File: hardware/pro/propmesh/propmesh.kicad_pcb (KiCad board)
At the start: 2 copper layers, 33 parts, among them J1 DC_IN, J2 DC_JACK, Q2 AOD4185, U1 TLV62569DBV, U2 AP64350SP-13

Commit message: Sheet 03 (slow outputs) captured + channel redesign to supply voltage
- LED-channel decision resolved: all 6 channels kept, discrete AO3400A
  low-side FETs (Basic, replaces sheet 06's 2N7002 too — one MOSFET
  part number board-wide); ULN2003 drives relays only
- Channels re-pointed +5V -> VIN_PROT with SS34 flyback per channel:
  2 A/ch, 5 A aggregate, 12/24 V lights and pneumatic solenoids are
  first-class loads. Supply-voltage coupling documented in the spec's
  user guidance (match supply to lights; mixed-voltage recipe)
- HK4100F relay: symbol+footprint imported, land pattern verified,
  EasyEDA inverted-pin defect fixed in library (4th known import lie,
  added to checklist); coil is 40 mA not 70; NO/NC continuity check
  deferred to bring-up by design
- checknet renderer: undrawn power rails annotate inside part boxes
  (no more +5V hairball); roll-call generalised
- All three drawn sheets: checknet green, ERC clean (31 one-sided
  labels pending sheets 04-07). Caught U3's footprint reverted to
  WROOM-1 by Update-from-Library field reset — reassigned, dialog
  gotcha documented

Co-Authored-By: Claude Fable 5 <noreply@anthropic.com>
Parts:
- added C13: 1u, Capacitor_SMD:C_0603_1608Metric, F.Cu at (149.2, 22.0)
- added C14: 100n, Capacitor_SMD:C_0603_1608Metric, F.Cu at (152.4, 26.7)
- added C15: 10u/16V, Capacitor_SMD:C_0805_2012Metric, F.Cu at (152.6, 52.8)
- added C16: 10U, Capacitor_SMD:C_0805_2012Metric, F.Cu at (253.6, 140.9)
- added C17: 100n, Capacitor_SMD:C_0603_1608Metric, F.Cu at (249.4, 117.7)
- added D10: SS34, Diode_SMD:D_SMA, F.Cu at (238.4, 136.9)
- added D11: SS34, Diode_SMD:D_SMA, F.Cu at (238.4, 141.4)
- added D5: SS34, Diode_SMD:D_SMA, F.Cu at (145.6, 46.4)
- added D6: SS34, Diode_SMD:D_SMA, F.Cu at (238.4, 118.7)
- added D7: SS34, Diode_SMD:D_SMA, F.Cu at (238.4, 123.2)
- added D8: SS34, Diode_SMD:D_SMA, F.Cu at (238.4, 127.8)
- added D9: SS34, Diode_SMD:D_SMA, F.Cu at (238.4, 132.3)
- added J10: SERVO, Connector_PinHeader_2.54mm:PinHeader_1x03_P2.54mm_Vertical, F.Cu at (245.8, 109.0)
- added J11: SERVO, Connector_PinHeader_2.54mm:PinHeader_1x03_P2.54mm_Vertical, F.Cu at (250.4, 109.0)
- added J12: SERVO, Connector_PinHeader_2.54mm:PinHeader_1x03_P2.54mm_Vertical, F.Cu at (255.0, 109.0)
- added J13: SERVO, Connector_PinHeader_2.54mm:PinHeader_1x03_P2.54mm_Vertical, F.Cu at (259.6, 109.0)
- added J3: RELAY_OUT, propmesh:CONN-TH_DG128-5.0-03P-14-00A-H, F.Cu at (226.2, 112.4)
- added J4: TYPE-C-31-M-12, Connector_USB:USB_C_Receptacle_HRO_TYPE-C-31-M-12, F.Cu at (127.0, 49.0)
- added J6: RELAY_OUT, propmesh:CONN-TH_DG128-5.0-03P-14-00A-H, F.Cu at (226.2, 123.8)
- added J7: SERVO, Connector_PinHeader_2.54mm:PinHeader_1x03_P2.54mm_Vertical, F.Cu at (236.7, 109.0)
- added J8: RELAY_OUT, propmesh:CONN-TH_DG128-5.0-03P-14-00A-H, F.Cu at (226.2, 135.3)
- added J9: SERVO, Connector_PinHeader_2.54mm:PinHeader_1x03_P2.54mm_Vertical, F.Cu at (241.2, 109.0)
- added J_LED1: LED_OUT, propmesh:CONN-TH_DG381S-3.5-02P-14-00A-H, F.Cu at (204.9, 100.4)
- added J_LED2: LED_OUT, propmesh:CONN-TH_DG381S-3.5-02P-14-00A-H, F.Cu at (213.6, 100.4)
- added J_LED3: LED_OUT, propmesh:CONN-TH_DG381S-3.5-02P-14-00A-H, F.Cu at (222.4, 100.4)
- added J_LED4: LED_OUT, propmesh:CONN-TH_DG381S-3.5-02P-14-00A-H, F.Cu at (231.1, 100.4)
- added J_LED5: LED_OUT, propmesh:CONN-TH_DG381S-3.5-02P-14-00A-H, F.Cu at (239.9, 100.4)
- added J_LED6: LED_OUT, propmesh:CONN-TH_DG381S-3.5-02P-14-00A-H, F.Cu at (248.6, 100.4)
- added K1: HK4100F-DC5V-SHG, propmesh:RELAY-TH_HK4100F-DC5V-SHG, F.Cu at (209.2, 112.9)
- added K2: HK4100F-DC5V-SHG, propmesh:RELAY-TH_HK4100F-DC5V-SHG, F.Cu at (209.2, 125.3)
- added K3: HK4100F-DC5V-SHG, propmesh:RELAY-TH_HK4100F-DC5V-SHG, F.Cu at (209.2, 137.6)
- added Q1: AO3400A, Package_TO_SOT_SMD:SOT-23, F.Cu at (244.9, 118.6)
- added Q3: AO3400A, Package_TO_SOT_SMD:SOT-23, F.Cu at (244.9, 123.1)
- added Q4: AO3400A, Package_TO_SOT_SMD:SOT-23, F.Cu at (244.9, 127.5)
- added Q5: AO3400A, Package_TO_SOT_SMD:SOT-23, F.Cu at (244.9, 132.0)
- added Q6: AO3400A, Package_TO_SOT_SMD:SOT-23, F.Cu at (244.9, 136.4)
- added Q7: AO3400A, Package_TO_SOT_SMD:SOT-23, F.Cu at (244.9, 140.9)
- added R10: 5.1k, Resistor_SMD:R_0603_1608Metric, F.Cu at (152.4, 29.2)
- added R11: 5.1k, Resistor_SMD:R_0603_1608Metric, F.Cu at (152.4, 31.7)
- added R12: 10k, Resistor_SMD:R_0603_1608Metric, F.Cu at (152.4, 34.2)
- added R13: 10k, Resistor_SMD:R_0603_1608Metric, F.Cu at (152.4, 36.7)
- added R14: 10k, Resistor_SMD:R_0603_1608Metric, F.Cu at (249.4, 120.2)
- added R15: 10k, Resistor_SMD:R_0603_1608Metric, F.Cu at (249.4, 122.7)
- added R16: 10k, Resistor_SMD:R_0603_1608Metric, F.Cu at (249.4, 125.2)
- added R17: 10k, Resistor_SMD:R_0603_1608Metric, F.Cu at (249.4, 127.7)
- added R18: 10k, Resistor_SMD:R_0603_1608Metric, F.Cu at (249.4, 130.2)
- added R19: 10k, Resistor_SMD:R_0603_1608Metric, F.Cu at (249.4, 132.7)
- added R20: 4.7k, Resistor_SMD:R_0603_1608Metric, F.Cu at (249.4, 135.2)
- added R21: 4.7k, Resistor_SMD:R_0603_1608Metric, F.Cu at (249.4, 137.8)
- added SW1: TS-1187A, Button_Switch_SMD:SW_Push_1P1T_XKB_TS-1187A, F.Cu at (171.5, 41.3)
- added SW2: TS-1187A, Button_Switch_SMD:SW_Push_1P1T_XKB_TS-1187A, F.Cu at (172.5, 54.5)
- added TP1: TP37, TestPoint:TestPoint_Pad_1.5x1.5mm, F.Cu at (148.4, 50.4)
- added U3: ESP32-S3-WROOM-1U-N8R2, RF_Module:ESP32-S3-WROOM-1U, F.Cu at (132.0, 24.7)
- added U4: USBLC6-2SC6, Package_TO_SOT_SMD:SOT-23-6, F.Cu at (144.1, 51.1)
- added U5: PCA9685PW, Package_SO:TSSOP-28_4.4x9.7mm_P0.65mm, F.Cu at (255.7, 133.8)
- added U6: ULN2003A, Package_SO:SOIC-16_3.9x9.9mm_P1.27mm, F.Cu at (255.6, 122.3)
- moved J2 34.6 mm to (18.9, 27.5)
- moved J1 22.3 mm to (18.0, 39.5), turned to -90 degrees
- moved F1 18.1 mm to (27.3, 10.3)
- moved C2 14.1 mm to (17.0, 51.0)
- moved Q2 12.9 mm to (46.8, 70.1)

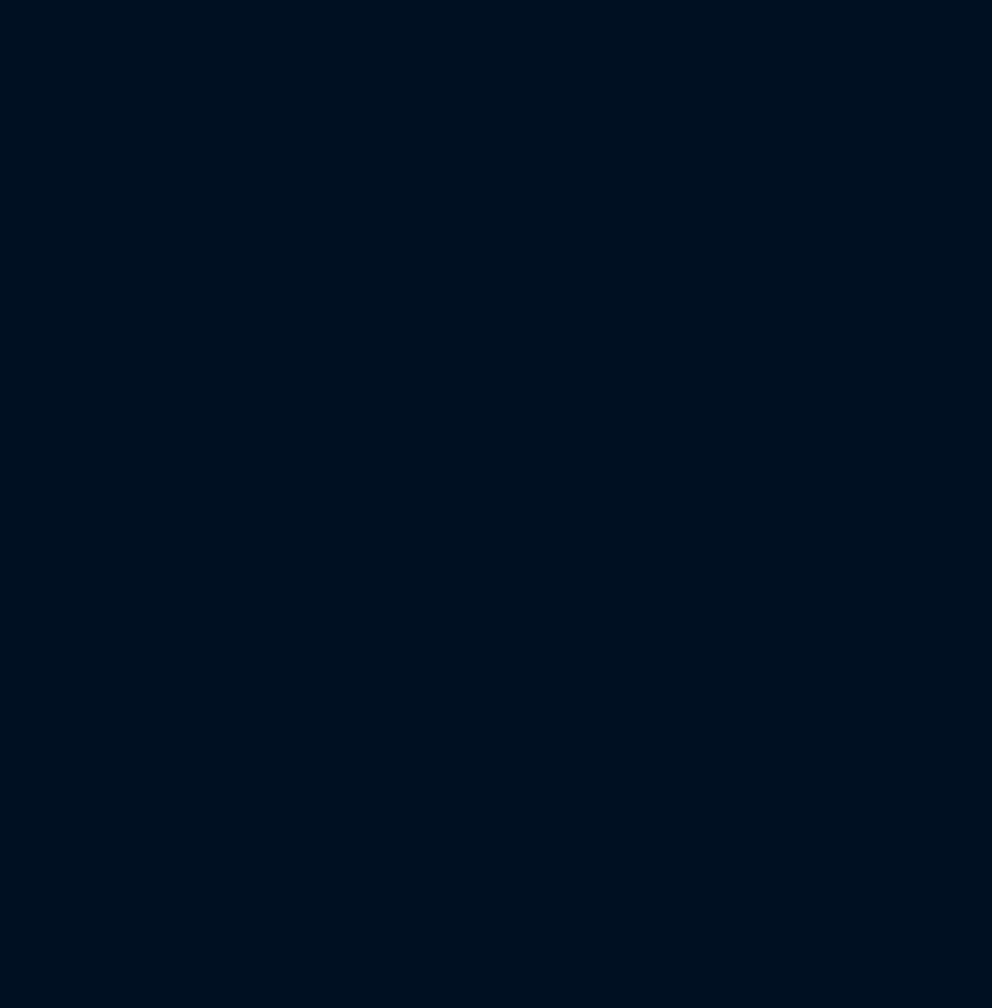
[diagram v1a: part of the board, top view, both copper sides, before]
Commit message: Sheet 04 (audio + SD) captured: mono amp, PCM5102A line-out, microSD
- MAX98357A config resolved datasheet-exact: GAIN_SLOT->GND = 12 dB
  (zero parts); SD_MODE mono mix via 620k to +3V3 (RLARGE formula,
  window computed vs trip points; rail chosen for noise margin and
  the one-rail strap convention). Genuine ADI $0.88@100 dissolved
  the clone question.
- Line-out dropped then REVERSED same day (Colin): PCM5102A second
  DAC on the shared I2S bus, TI Fig.33 literal (SCK grounded = BCK
  PLL), 470R+2.2nF outputs, PJ-320A jack. ~$1.65 for the honest
  version; audio block $3.28@100 verified vs $2.65 estimate.
- PJ-320A mapping settled by geometry after THREE numbering schemes
  collided (datasheet contacts 1-4, import pads 2-5, unnumbered PCB
  layout): L=4 (deepest spring = tip, Colin's argument), R=3,
  GND=2+5. Meter-confirm at bring-up. Import-lie #5 documented.
- microSD TF-01A with D3 pull-up ADDED beyond the pinmap note
  (ESP-IDF: D3 low drops the card into SPI mode); card-detect to a
  test pad.
- Library: pin types set on all four audio imports (amp NC pins
  typed no_connect); peg-hole NPTH fixes on TF-01A and PJ-320A.
- checknet renderer: rail-only parts (pure decoupling) now render in
  their own diagram section — ten invisible caps taught us the
  drawing guide could silently drop parts.
- All four drawn sheets: checknet green, ERC clean.

Co-Authored-By: Claude Fable 5 <noreply@anthropic.com>
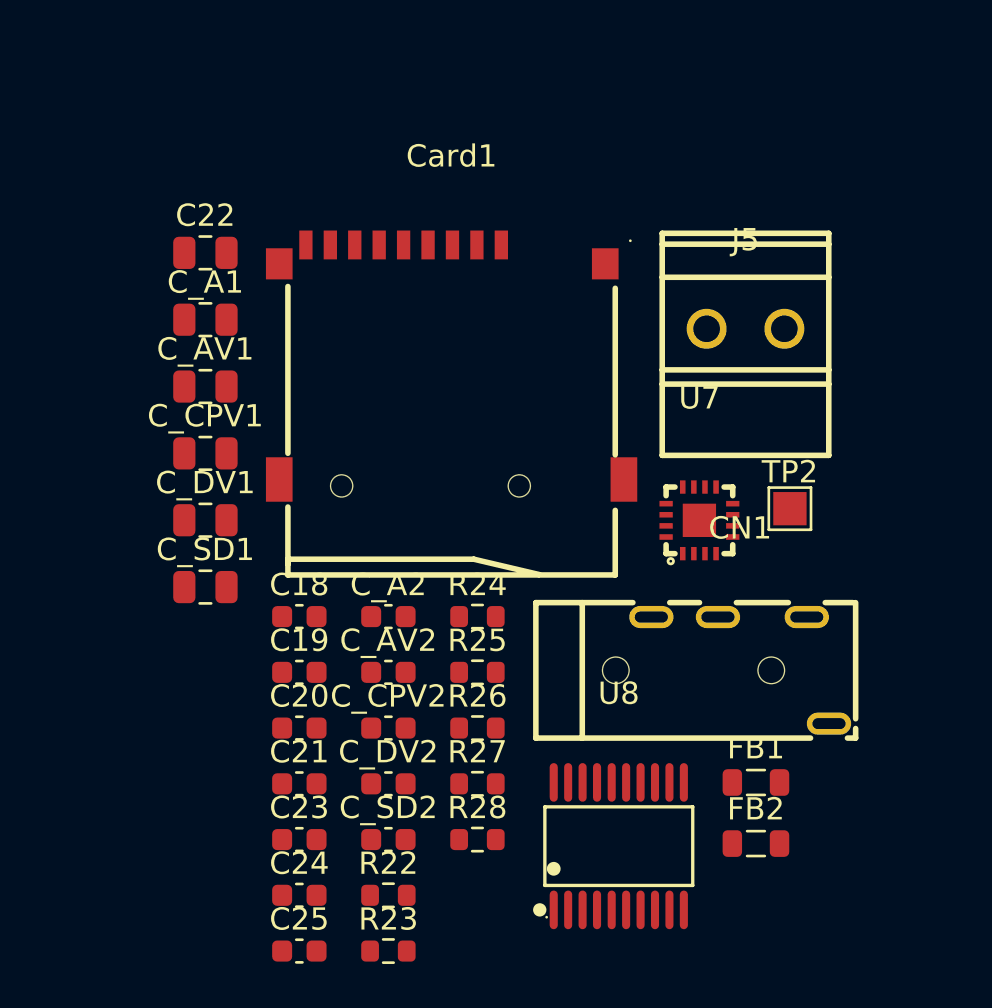
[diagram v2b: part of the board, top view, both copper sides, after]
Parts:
- added C18: 100p, Capacitor_SMD:C_0603_1608Metric, F.Cu at (33.0, 169.4)
- added C19: 100p, Capacitor_SMD:C_0603_1608Metric, F.Cu at (33.0, 171.9)
- added C20: 2.2u, Capacitor_SMD:C_0603_1608Metric, F.Cu at (33.0, 174.4)
- added C21: 2.2u, Capacitor_SMD:C_0603_1608Metric, F.Cu at (33.0, 176.9)
- added C22: 10u, Capacitor_SMD:C_0805_2012Metric, F.Cu at (28.7, 153.0)
- added C23: 100n, Capacitor_SMD:C_0603_1608Metric, F.Cu at (33.0, 179.4)
- added C24: 2.2n, Capacitor_SMD:C_0603_1608Metric, F.Cu at (33.0, 181.9)
- added C25: 2.2n, Capacitor_SMD:C_0603_1608Metric, F.Cu at (33.0, 184.4)
- added CN1: LINE_OUT, propmesh:AUDIO-TH_XKB_PJ-320A, F.Cu at (52.8, 171.8)
- added C_A1: 10u, Capacitor_SMD:C_0805_2012Metric, F.Cu at (28.7, 156.0)
- added C_A2: 100n, Capacitor_SMD:C_0603_1608Metric, F.Cu at (37.0, 169.4)
- added C_AV1: 10u, Capacitor_SMD:C_0805_2012Metric, F.Cu at (28.7, 159.0)
- added C_AV2: 100n, Capacitor_SMD:C_0603_1608Metric, F.Cu at (37.0, 171.9)
- added C_CPV1: 10u, Capacitor_SMD:C_0805_2012Metric, F.Cu at (28.7, 162.0)
- added C_CPV2: 100n, Capacitor_SMD:C_0603_1608Metric, F.Cu at (37.0, 174.4)
- added C_DV1: 10u, Capacitor_SMD:C_0805_2012Metric, F.Cu at (28.7, 165.0)
- added C_DV2: 100n, Capacitor_SMD:C_0603_1608Metric, F.Cu at (37.0, 176.9)
- added C_SD1: 10u, Capacitor_SMD:C_0805_2012Metric, F.Cu at (28.7, 168.1)
- added C_SD2: 100n, Capacitor_SMD:C_0603_1608Metric, F.Cu at (37.0, 179.4)
- added Card1: TF-01A, propmesh:TF-SMD_TF-01A, F.Cu at (39.8, 157.9)
- added FB1: BLM21PG221SN1D, Inductor_SMD:L_0805_2012Metric, F.Cu at (53.5, 176.9)
- added FB2: BLM21PG221SN1D, Inductor_SMD:L_0805_2012Metric, F.Cu at (53.5, 179.6)
- added J5: SPEAKER, propmesh:CONN-TH_DG381S-3.5-02P-14-00A-H, F.Cu at (53.0, 156.4)
- added R22: 620K, Resistor_SMD:R_0603_1608Metric, F.Cu at (37.0, 181.9)
- added R23: 10k, Resistor_SMD:R_0603_1608Metric, F.Cu at (37.0, 184.4)
- added R24: 470, Resistor_SMD:R_0603_1608Metric, F.Cu at (41.0, 169.4)
- added R25: 470, Resistor_SMD:R_0603_1608Metric, F.Cu at (41.0, 171.9)
- added R26: 10k, Resistor_SMD:R_0603_1608Metric, F.Cu at (41.0, 174.4)
- added R27: 10k, Resistor_SMD:R_0603_1608Metric, F.Cu at (41.0, 176.9)
- added R28: 10k, Resistor_SMD:R_0603_1608Metric, F.Cu at (41.0, 179.4)
- added TP2: TP_CD, TestPoint:TestPoint_Pad_1.5x1.5mm, F.Cu at (55.0, 164.5)
- added U7: MAX98357AETE+T, propmesh:TQFN-16_L3.0-W3.0-P0.50-BL-EP1.5, F.Cu at (51.0, 165.1)
- added U8: PCM5102APWR, propmesh:TSSOP-20_L6.5-W4.4-P0.65-LS6.4-BL, F.Cu at (47.3, 179.7)

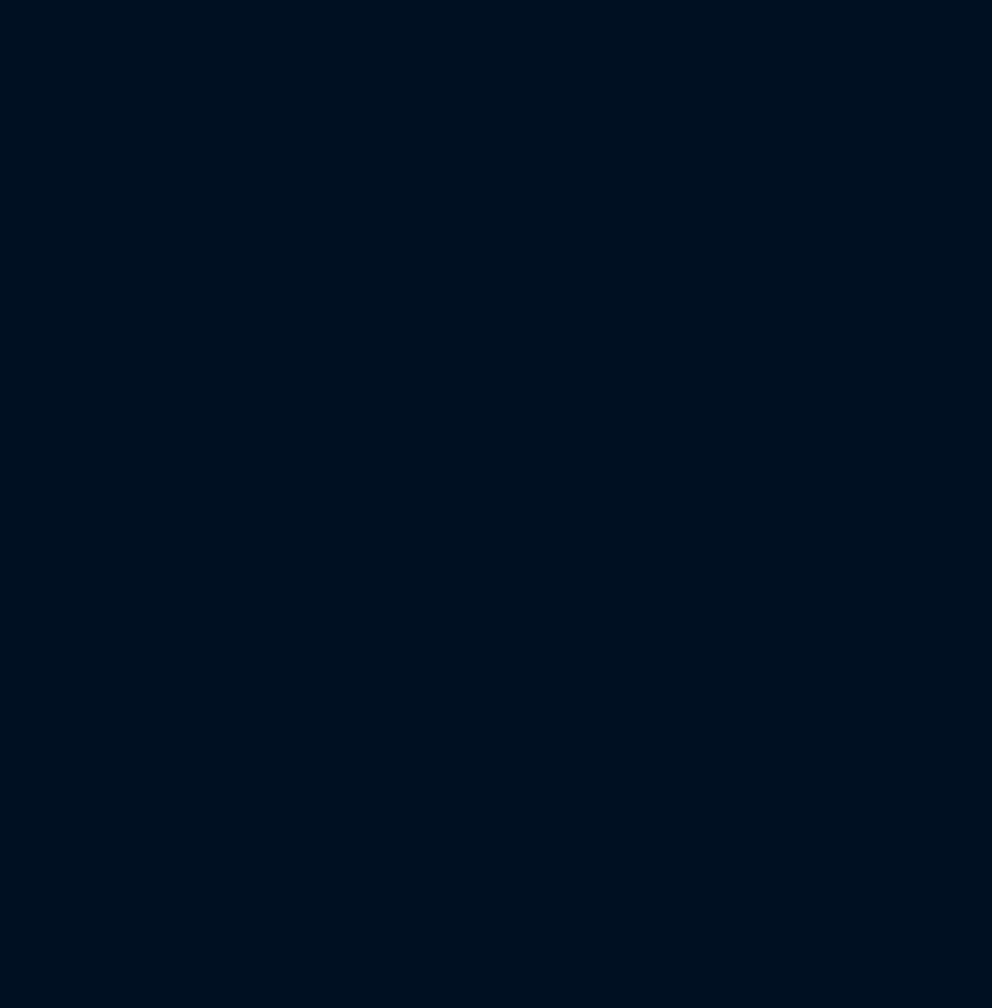
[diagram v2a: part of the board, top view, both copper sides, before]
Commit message: Sheet 06 (motors) captured: stepper sockets + DRV8871, all spec unknowns closed
- Open item #3 CLOSED from the Pololu md09b drawing: StepStick rows
  12.70 mm apart exactly, 1x8 @ 2.54; RST/SLP positions hardwired
  together = A4988-legal AND the TMC2209 PDN_UART bus (shared, both
  sockets, MS1/MS2 straps = addresses); DIAG via per-socket aux
  headers + bridged solder jumpers (vendor positions differ);
  1k series on GPIO43 (U0TXD boot log)
- ILIM verified from TI DS: ITRIP = 64000/R; 30k = 2.13 A/channel
- Import lie #6 caught: DRV8871's generic footprint name collided
  with the AP64350's and --overwrite silently replaced it (geometry
  happened to be identical; only the LCSC property flipped). Restored
  + forked to SO-8EP_DRV8871DDAR; post-import git-status rule added
- checknet: name-aware tie-breaks — six identical strap headers on
  six identically-shaped nets defeated value-level pairing and
  reported phantom crosses on a perfectly-wired sheet; user labels
  now arbitrate ties. All five drawn sheets re-verified green
- DRV8871 pin types set in library; ERC clean board-wide
- Motor block $4.75@100 verified (DRV8871 genuine = 2x the old
  estimate); duty-paid ~$49.52. CLAUDE.md verification item #3 closed
  (last hardware unknown in the spec)

Co-Authored-By: Claude Fable 5 <noreply@anthropic.com>
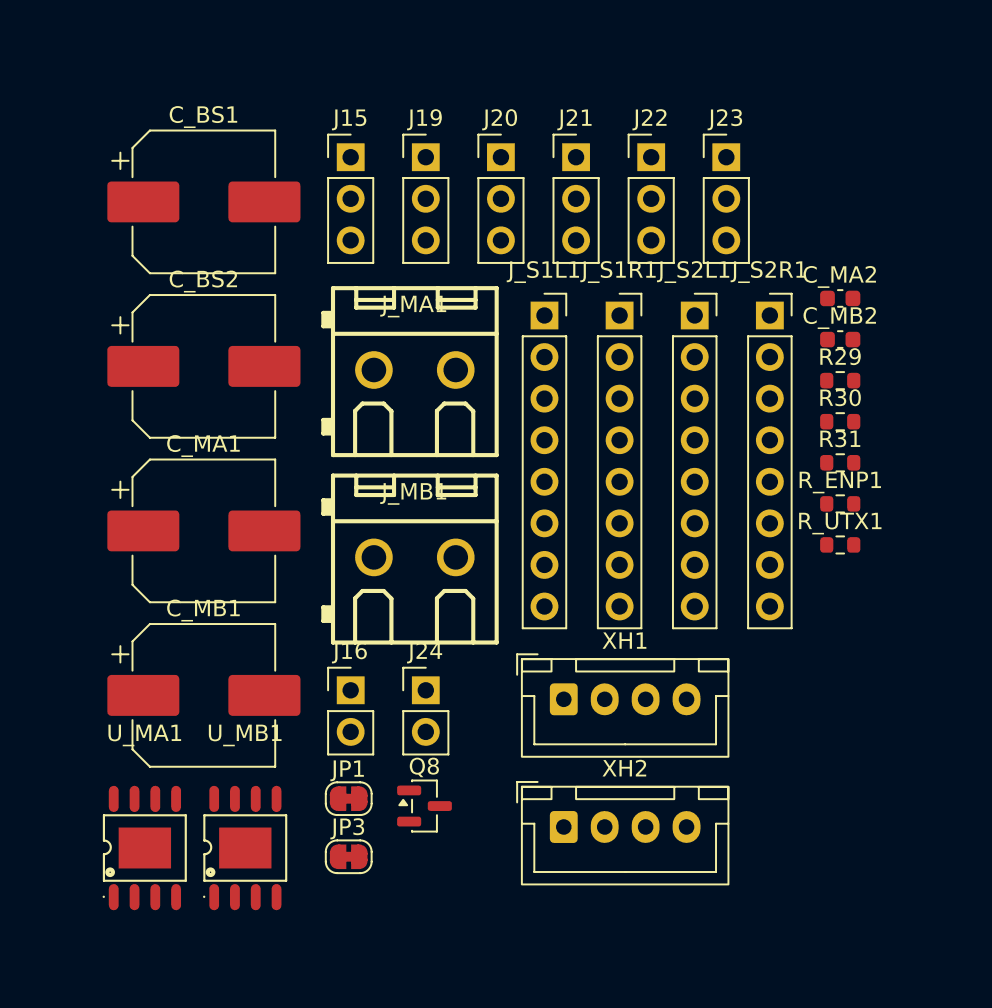
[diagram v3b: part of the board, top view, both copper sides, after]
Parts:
- added C_BS1: 100u/63V, Capacitor_SMD:CP_Elec_8x10.5, F.Cu at (111.7, 126.0)
- added C_BS2: 100u/63V, Capacitor_SMD:CP_Elec_8x10.5, F.Cu at (111.7, 136.1)
- added C_MA1: 100u/63V, Capacitor_SMD:CP_Elec_8x10.5, F.Cu at (111.7, 146.1)
- added C_MA2: 100n, Capacitor_SMD:C_0603_1608Metric, F.Cu at (150.6, 131.9)
- added C_MB1: 100u/63V, Capacitor_SMD:CP_Elec_8x10.5, F.Cu at (111.7, 156.2)
- added C_MB2: 100n, Capacitor_SMD:C_0603_1608Metric, F.Cu at (150.6, 134.4)
- added J15: MS_SEL, Connector_PinHeader_2.54mm:PinHeader_1x03_P2.54mm_Vertical, F.Cu at (120.6, 123.3)
- added J16: DIAG_AUX, Connector_PinHeader_2.54mm:PinHeader_1x02_P2.54mm_Vertical, F.Cu at (120.6, 155.9)
- added J19: MS_SEL, Connector_PinHeader_2.54mm:PinHeader_1x03_P2.54mm_Vertical, F.Cu at (125.2, 123.3)
- added J20: MS_SEL, Connector_PinHeader_2.54mm:PinHeader_1x03_P2.54mm_Vertical, F.Cu at (129.8, 123.3)
- added J21: MS_SEL, Connector_PinHeader_2.54mm:PinHeader_1x03_P2.54mm_Vertical, F.Cu at (134.4, 123.3)
- added J22: MS_SEL, Connector_PinHeader_2.54mm:PinHeader_1x03_P2.54mm_Vertical, F.Cu at (139.0, 123.3)
- added J23: MS_SEL, Connector_PinHeader_2.54mm:PinHeader_1x03_P2.54mm_Vertical, F.Cu at (143.6, 123.3)
- added J24: DIAG_AUX, Connector_PinHeader_2.54mm:PinHeader_1x02_P2.54mm_Vertical, F.Cu at (125.2, 155.9)
- added JP1: SJ, Jumper:SolderJumper-2_P1.3mm_Bridged_RoundedPad1.0x1.5mm, F.Cu at (120.5, 162.5)
- added JP3: SJ, Jumper:SolderJumper-2_P1.3mm_Bridged_RoundedPad1.0x1.5mm, F.Cu at (120.5, 166.0)
- added J_MA1: MOTOR_OUT, propmesh:CONN-TH_DG128-5.0-02P-14-00A-H, F.Cu at (124.6, 136.3)
- added J_MB1: MOTOR_OUT, propmesh:CONN-TH_DG128-5.0-02P-14-00A-H, F.Cu at (124.6, 147.7)
- added J_S1L1: SOCKET_1x8, Connector_PinSocket_2.54mm:PinSocket_1x08_P2.54mm_Vertical, F.Cu at (132.5, 133.0)
- added J_S1R1: SOCKET_1x8, Connector_PinSocket_2.54mm:PinSocket_1x08_P2.54mm_Vertical, F.Cu at (137.1, 133.0)
- added J_S2L1: SOCKET_1x8, Connector_PinSocket_2.54mm:PinSocket_1x08_P2.54mm_Vertical, F.Cu at (141.7, 133.0)
- added J_S2R1: SOCKET_1x8, Connector_PinSocket_2.54mm:PinSocket_1x08_P2.54mm_Vertical, F.Cu at (146.3, 133.0)
- added Q8: AO3400A, Package_TO_SOT_SMD:SOT-23, F.Cu at (125.2, 162.9)
- added R29: 1k, Resistor_SMD:R_0603_1608Metric, F.Cu at (150.6, 136.9)
- added R30: 30k, Resistor_SMD:R_0603_1608Metric, F.Cu at (150.6, 139.5)
- added R31: 30k, Resistor_SMD:R_0603_1608Metric, F.Cu at (150.6, 142.0)
- added R_ENP1: 10k, Resistor_SMD:R_0603_1608Metric, F.Cu at (150.6, 144.5)
- added R_UTX1: 1k, Resistor_SMD:R_0603_1608Metric, F.Cu at (150.6, 147.0)
- added U_MA1: DRV8871DDAR, propmesh:SO-8EP_DRV8871DDAR, F.Cu at (108.1, 165.5)
- added U_MB1: DRV8871DDAR, propmesh:SO-8EP_DRV8871DDAR, F.Cu at (114.2, 165.5)
- added XH1: STEPPER_COIL, Connector_JST:JST_XH_B4B-XH-A_1x04_P2.50mm_Vertical, F.Cu at (133.7, 156.4)
- added XH2: STEPPER_COIL, Connector_JST:JST_XH_B4B-XH-A_1x04_P2.50mm_Vertical, F.Cu at (133.7, 164.2)
